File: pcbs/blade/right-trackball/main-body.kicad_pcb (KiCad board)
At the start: 2 copper layers, 133 x 90.1 mm, 88 parts, among them J1 expantion1, J11 Conn_01x04_Female, J12 USB-C USB 2.0 MC-372, J16 Conn_01x03_Male, J9 Conn_Display_general, Q1 AO3407, Q2 AO3407, SW1 SW_PUSH-kbd, SW10 SW_PUSH-kbd, SW11 SW_PUSH-kbd, SW12 SW_PUSH-kbd, SW14 SW_PUSH-kbd, SW15 SW_PUSH-kbd, SW16 SW_PUSH-kbd, SW17 SW_PUSH-kbd, SW18 SW_PUSH-kbd, SW2 SW_PUSH-kbd, SW20 SW_PUSH-kbd, SW3 SW_PUSH-kbd, SW4 SW_PUSH-kbd, SW5 SW_PUSH-kbd, SW6 SW_PUSH-kbd, SW7 SW_PUSH-kbd, SW8 SW_PUSH-kbd, SW9 SW_PUSH-kbd, U1 E73-2G4M08S1C, U2 SRV05-4, U3 XC6220B331MR-G, U4 MAX17048, U5 TP4054, U8 CAP1203, X1 32.768 kHz

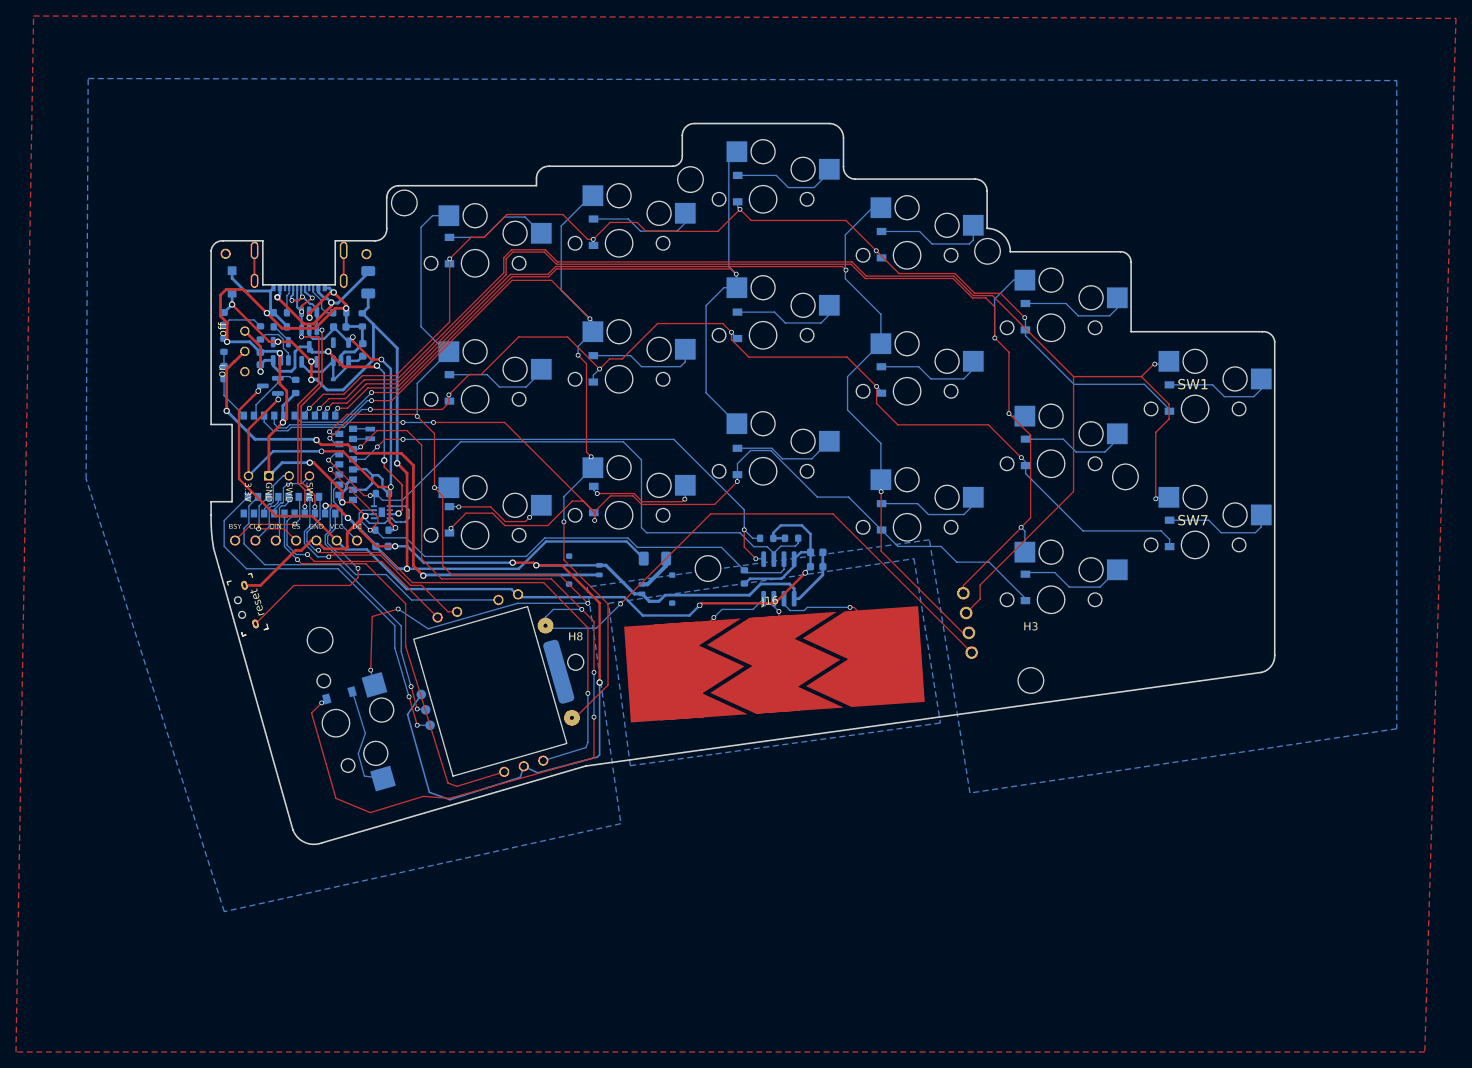
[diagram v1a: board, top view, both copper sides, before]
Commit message: add blade right with only keys (3x5)
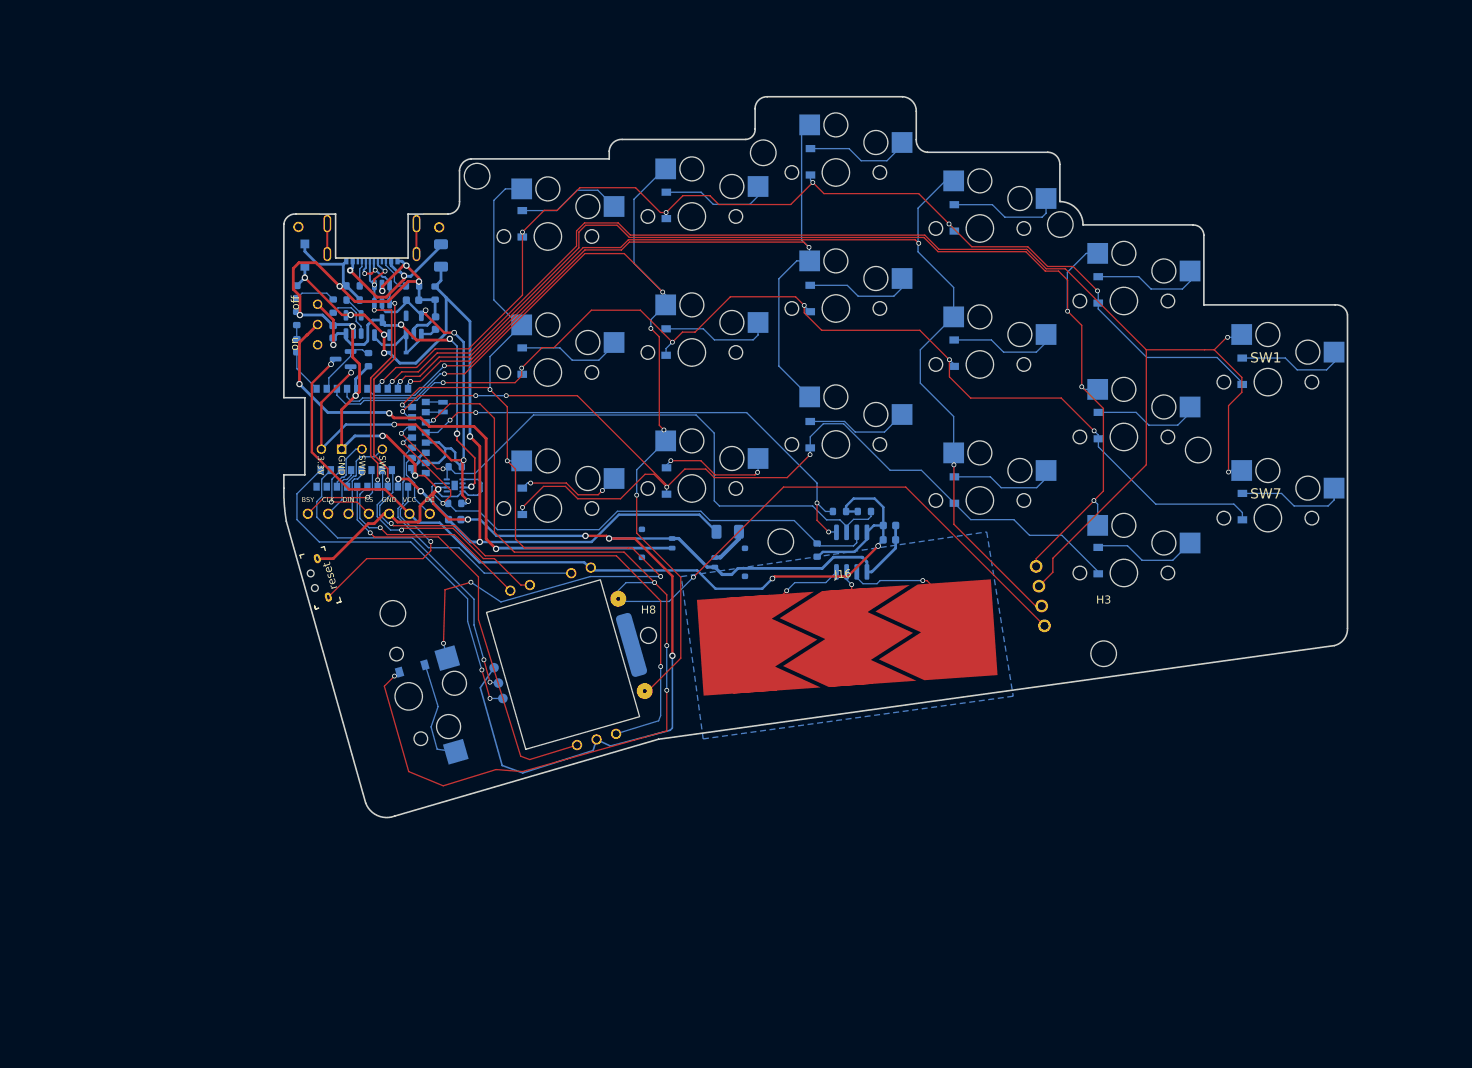
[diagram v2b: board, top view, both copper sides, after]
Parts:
- moved C1 9.69 mm to (101.2, 97.6)
- moved C14 9.69 mm to (155.5, 100.1)
- moved D1 9.69 mm to (199.6, 79.0)
- moved D10 9.69 mm to (145.6, 69.9)
- moved D14 9.69 mm to (181.6, 102.7)
- moved D15 9.69 mm to (163.6, 93.9)
- moved D16 9.69 mm to (145.6, 86.9)
- moved D2 9.69 mm to (181.6, 68.8)
- moved D22 9.69 mm to (94.1, 76.7)
- moved D23 9.69 mm to (81.5, 75.8)
- moved D24 9.69 mm to (81.5, 69.1)
- moved D25 9.69 mm to (82.5, 64.5)
- moved D3 9.69 mm to (163.6, 59.8)
- moved D5 9.69 mm to (127.6, 58.3)
- moved D7 9.69 mm to (199.6, 95.9)
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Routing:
- net (no net): track 3166.4 -> 3165.6 mm
- removed copper zone on F.Cu, net (none)
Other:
- outline, holes or cut-outs redrawn
